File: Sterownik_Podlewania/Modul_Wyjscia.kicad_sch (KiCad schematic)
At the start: 10 parts, among them J2 Screw_Terminal_01x02, K2 SANYOU_SRD_Form_C, Q2 BC547, SW8 SW_Nidec_CAS-120A1

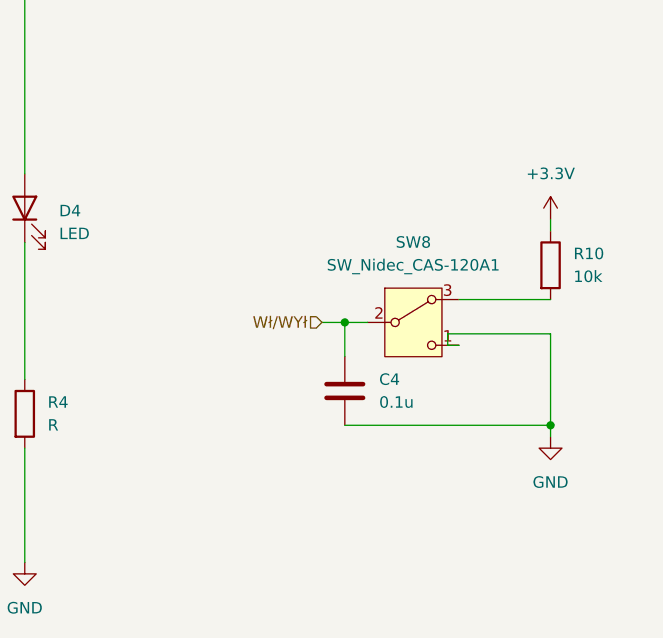
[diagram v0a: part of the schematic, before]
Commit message: Dodanie dokumentacji przełączników, sprawdzenie konwertera I2C, dodanie sekcji przełącznika, dodanie DIP swticha do przełączania zasialania zew, wydzielenie sekcji zasilania
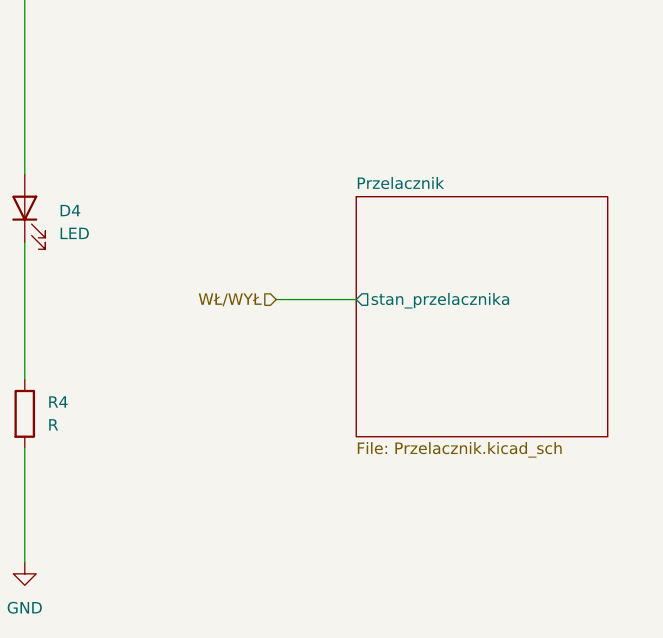
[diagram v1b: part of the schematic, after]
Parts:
- removed C4: 0.1u, Capacitor_SMD:C_1206_3216Metric, symbol Device:C
- removed R10: 10k, Resistor_SMD:R_1206_3216Metric, symbol Device:R
- removed SW8: SW_Nidec_CAS-120A1, Button_Switch_SMD:Nidec_Copal_CAS-120A, symbol Switch:SW_Nidec_CAS-120A1
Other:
- added sheet Przelacznik (Przelacznik.kicad_sch)

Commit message: Poprawki estetyczne schematu
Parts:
- R3: value R -> 680
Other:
- moved on the sheet: D3, D4, J2, K2, Q2, R3, R4

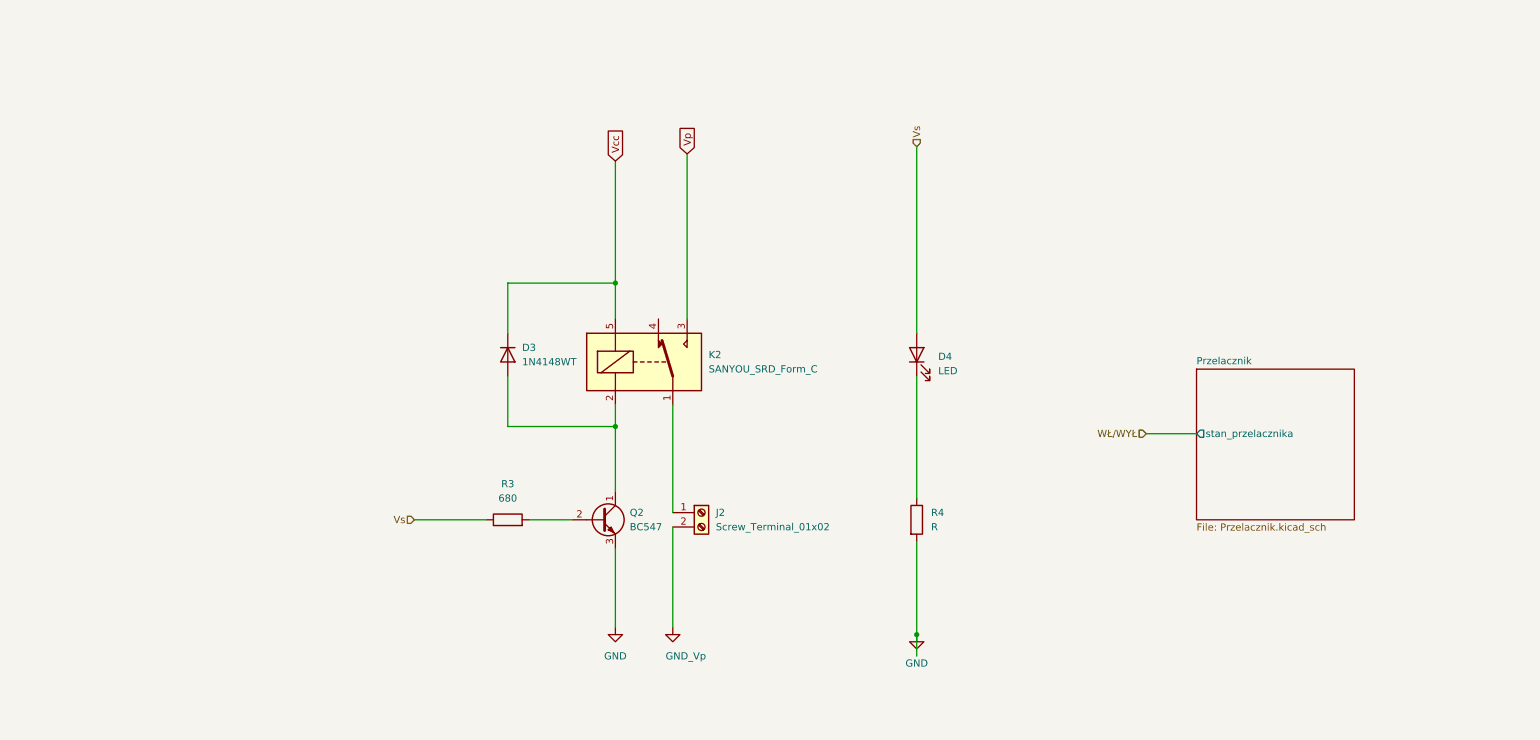
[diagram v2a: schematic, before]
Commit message: Dodanie gniazd ethernet, poprawienie większośc ERC
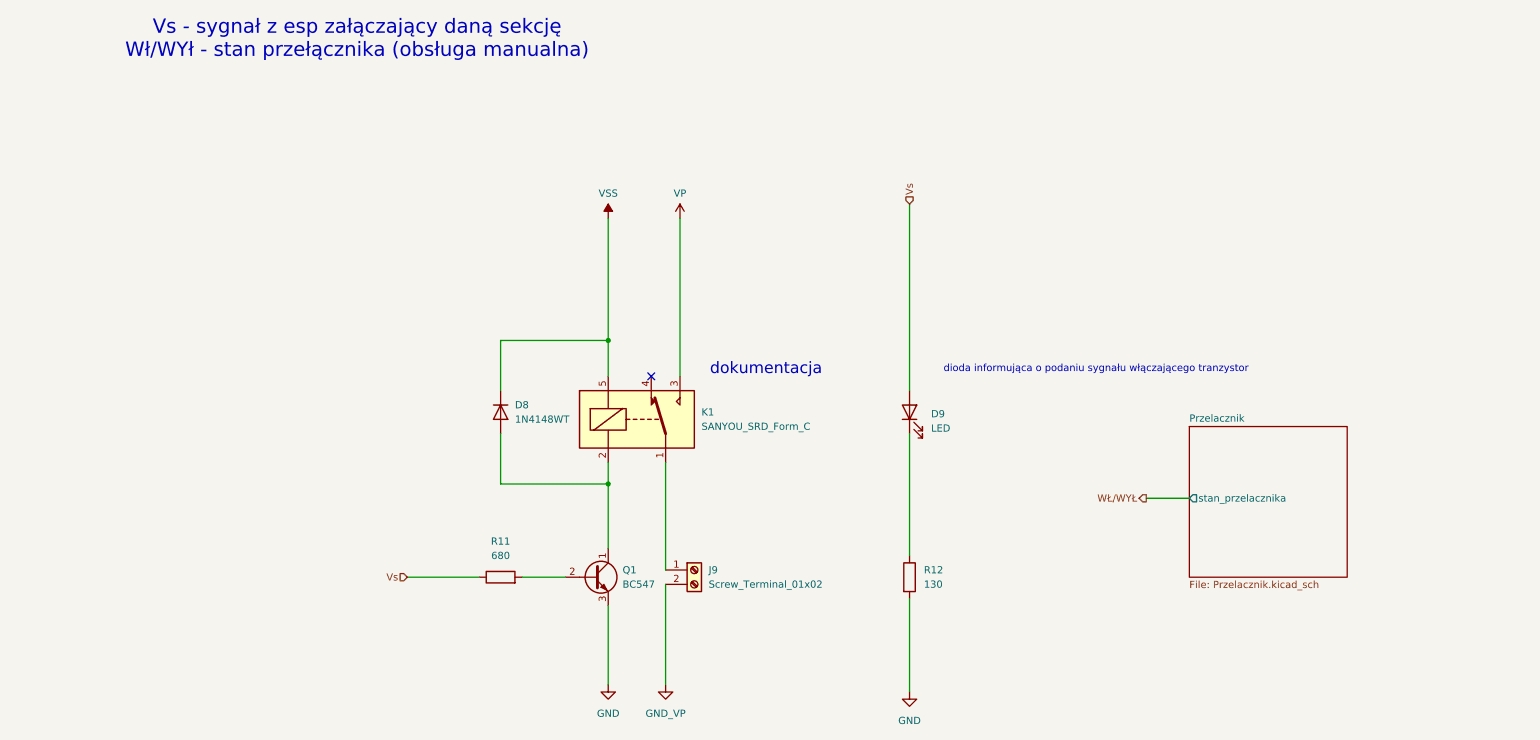
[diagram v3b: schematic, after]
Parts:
- R12: renamed from R4; value R -> 130
- renumbered D3 to D8, D4 to D9, J2 to J9, K2 to K1, Q2 to Q1, R3 to R11
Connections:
- net GND_Vp renamed GND_VP
- net Vcc renamed VSS
- net Vp renamed VP
- no-connect marks 0 -> 1
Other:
- note added: "Vs - sygnał z esp załączający daną sekcję Wł/WYł - stan przełącznika (obsługa manualna)"
- note added: "dioda informująca o podaniu sygnału włączającego tranzystor"
- note added: "dokumentacja"
- title: (none) -> Sterownik podlewania V1.1
- moved on the sheet: D8, D9, J9, K1, Q1, R11, R12

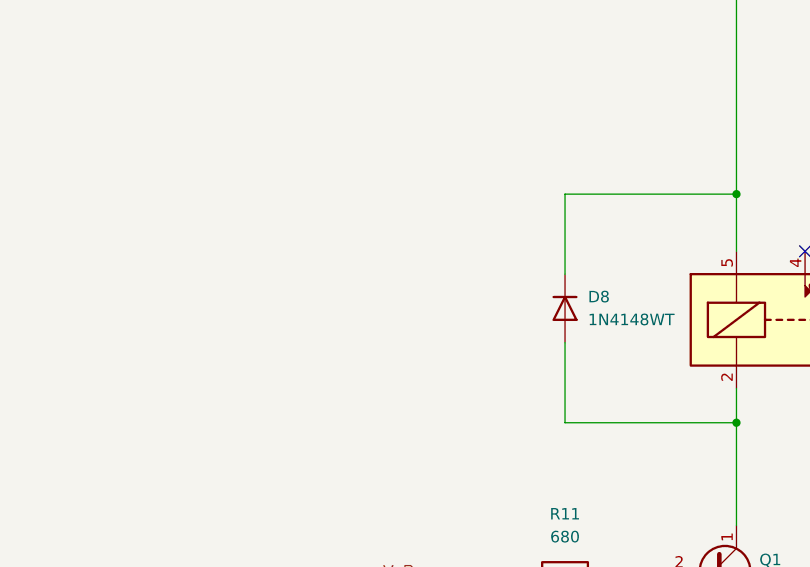
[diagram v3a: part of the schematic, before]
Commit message: Zmiana footprintó diód przekaźnika na schottky,finalne ułożenie  przekaźników, diód itp
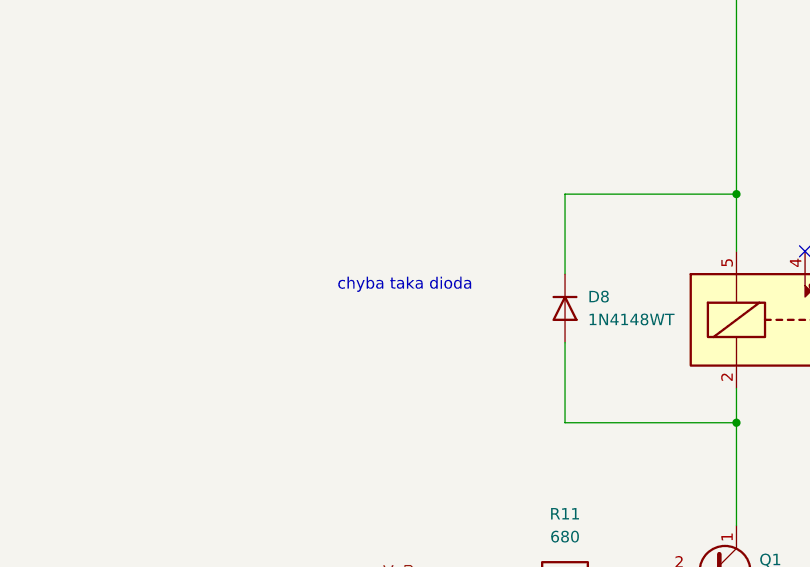
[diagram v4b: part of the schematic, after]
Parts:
- D8: footprint Diode_SMD:D_SOD-523 -> Diode_SMD:D_1206_3216Metric
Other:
- note added: "chyba taka dioda"
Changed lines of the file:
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@@
+		)
+	)
+	(text "chyba taka dioda"
+		(exclude_from_sim no)
+		(at 72.39 88.9 0)
+		(effects
+			(font
+				(size 1.27 1.27)
+			)
+			(href "https://www.tme.eu/pl/details/sd1206s100s1r0/diody-schottky-smd/kyocera-avx/")
 		)
 	)
@@
 			)
 		)
-		(property "Footprint" "Diode_SMD:D_SOD-523"
+		(property "Footprint" "Diode_SMD:D_1206_3216Metric"
 			(at 85.725 91.44 0)
 			(effects
